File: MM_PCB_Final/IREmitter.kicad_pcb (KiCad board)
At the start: 2 copper layers, 94 x 92.6 mm, 73 parts, among them J1 PPTC041LFBN-RC, J2 Conn_01x06, J3 Conn_01x06, J7 JST Connector, J8 JST Connector, Q1 IR Receiver, Q2 IR Receiver, Q3 IR Receiver, Q4 IR Receiver, SW2 Switch, U1 MOSFET, U2 MOSFET, U3 MOSFET, U4 MOSFET, U5 STM32F205RGTx, U7 H-Bridge, U8 Voltage Regulator

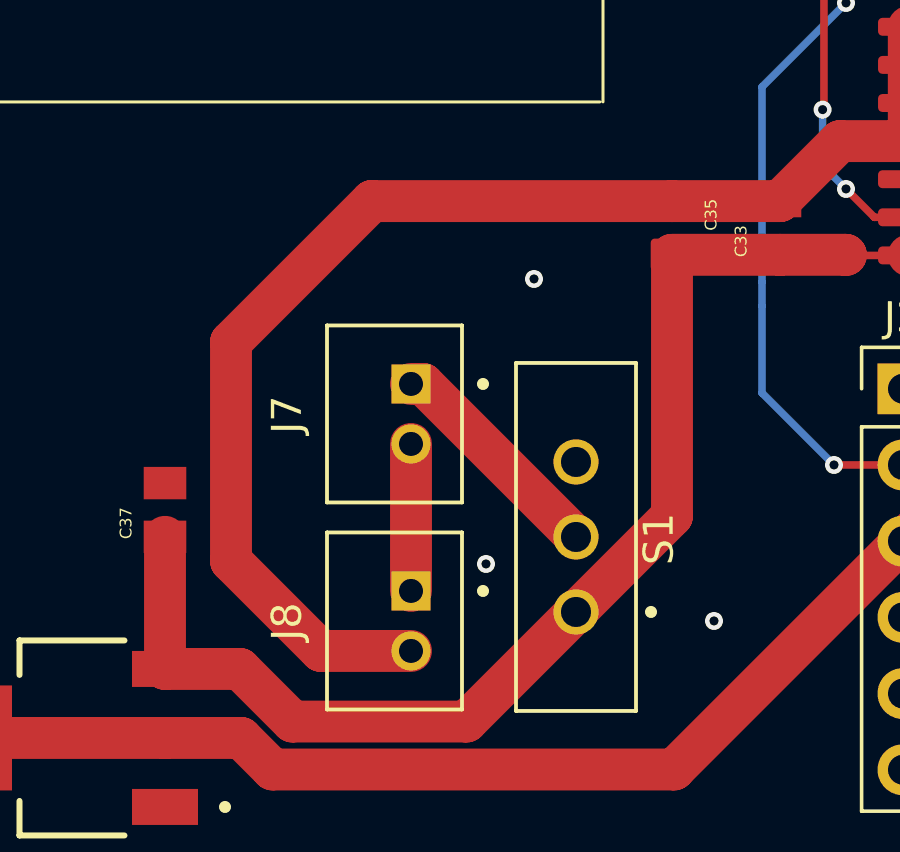
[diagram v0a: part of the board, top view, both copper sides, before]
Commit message: fix mgnd and gnd short
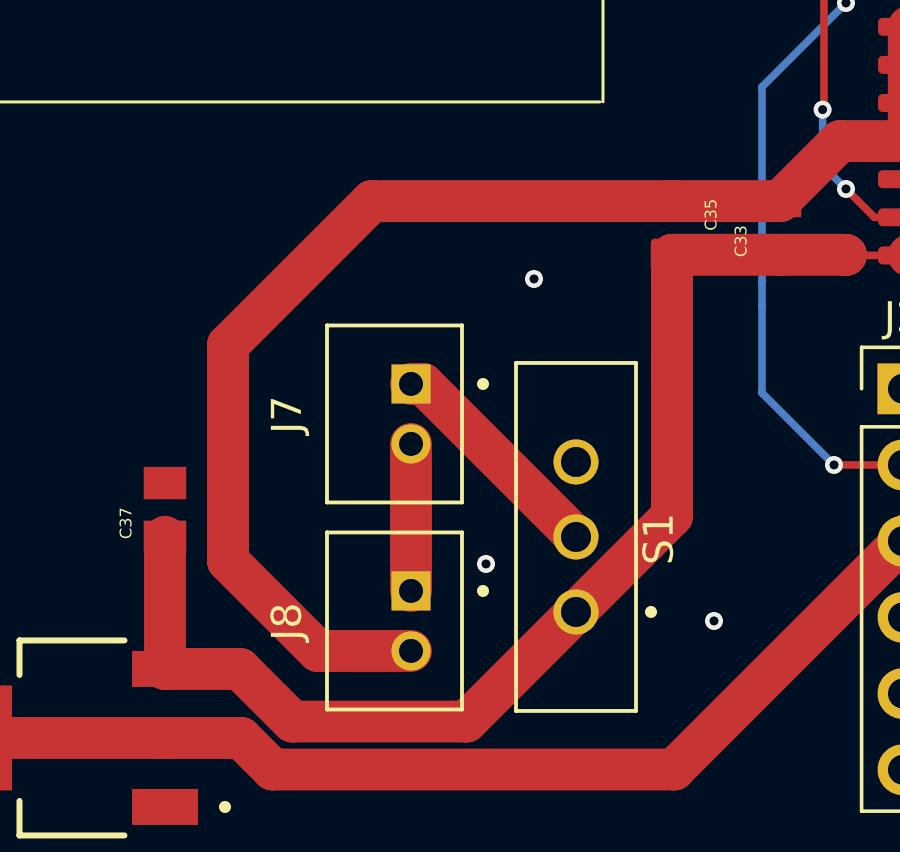
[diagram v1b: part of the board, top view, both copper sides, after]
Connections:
- J8 pad 2: GND -> MGND
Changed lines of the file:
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@@
 			(layers "*.Cu" "*.Mask")
 			(remove_unused_layers no)
-			(net 2 "GND")
+			(net 4 "MGND")
 			(pinfunction "2")
 			(pintype "passive")
@@
 	)
 	(segment
-		(start 121.3 97.3)
-		(end 116.6 102)
-		(width 1.397)
-		(layer "F.Cu")
-		(net 4)
-	)
-	(segment
-		(start 121.305 97.305)
-		(end 121.3 97.3)
+		(start 119.5 112.3)
+		(end 116.5 109.3)
 		(width 1.397)
 		(layer "F.Cu")
@@
 	)
 	(segment
-		(start 116.6 109.3)
-		(end 119.6 112.3)
+		(start 116.5 102.1)
+		(end 121.295 97.305)
 		(width 1.397)
 		(layer "F.Cu")
@@
 	)
 	(segment
-		(start 139.1925 95.305)
-		(end 136.9 95.305)
+		(start 116.5 109.3)
+		(end 116.5 102.1)
 		(width 1.397)
 		(layer "F.Cu")
@@
 	)
 	(segment
-		(start 139.1925 91.495)
-		(end 139.1925 95.305)
+		(start 121.295 97.305)
+		(end 131.3 97.305)
 		(width 1.397)
 		(layer "F.Cu")
@@
 	)
 	(segment
-		(start 141.765 94.035)
-		(end 141.8 94)
+		(start 139.1925 95.305)
+		(end 136.9 95.305)
 		(width 1.397)
 		(layer "F.Cu")
@@
 	)
 	(segment
-		(start 119.6 112.3)
-		(end 122.6 112.3)
+		(start 139.1925 91.495)
+		(end 139.1925 95.305)
 		(width 1.397)
 		(layer "F.Cu")
@@
 	)
 	(segment
-		(start 148.5025 91.495)
-		(end 148.5025 95.305)
+		(start 141.765 94.035)
+		(end 141.8 94)
 		(width 1.397)
 		(layer "F.Cu")
@@
 	)
 	(segment
-		(start 131.3 97.305)
-		(end 121.305 97.305)
+		(start 148.5025 91.495)
+		(end 148.5025 95.305)
 		(width 1.397)
 		(layer "F.Cu")
@@
 	)
 	(segment
-		(start 116.6 102)
-		(end 116.6 109.3)
+		(start 139.1925 94.035)
+		(end 141.765 94.035)
 		(width 1.397)
 		(layer "F.Cu")
@@
 	)
 	(segment
-		(start 139.1925 94.035)
-		(end 141.765 94.035)
+		(start 145.7 94)
+		(end 148.4675 94)
 		(width 1.397)
 		(layer "F.Cu")
@@
 	)
 	(segment
-		(start 145.7 94)
-		(end 148.4675 94)
+		(start 122.6 112.3)
+		(end 119.5 112.3)
 		(width 1.397)
 		(layer "F.Cu")
